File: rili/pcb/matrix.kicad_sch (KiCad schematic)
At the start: 144 parts, among them J5 MJ-4PP-9, P5 i2c-pin, P6 i2c-pin, SW100 SW_PUSH, SW101 SW_PUSH, SW102 SW_PUSH, SW103 SW_PUSH, SW104 SW_PUSH, SW105 SW_PUSH, SW54 SW_PUSH, SW55 SW_PUSH, SW56 SW_PUSH, SW57 SW_PUSH, SW58 SW_PUSH, SW59 SW_PUSH, SW60 SW_PUSH, SW61 SW_PUSH, SW62 SW_PUSH, SW63 SW_PUSH, SW64 SW_PUSH, SW65 SW_PUSH, SW66 SW_PUSH, SW67 SW_PUSH, SW68 SW_PUSH, SW69 SW_PUSH, SW70 SW_PUSH, SW71 SW_PUSH, SW72 SW_PUSH, SW73 SW_PUSH, SW74 SW_PUSH, SW75 SW_PUSH, SW76 SW_PUSH, SW77 SW_PUSH, SW78 SW_PUSH, SW79 SW_PUSH, SW80 SW_PUSH, SW81 SW_PUSH, SW82 SW_PUSH, SW83 SW_PUSH, SW84 SW_PUSH, SW85 SW_PUSH, SW86 SW_PUSH, SW87 SW_PUSH, SW88 SW_PUSH, SW89 SW_PUSH, SW90 SW_PUSH, SW91 SW_PUSH, SW92 SW_PUSH, SW93 SW_PUSH, SW94 SW_PUSH, SW95 SW_PUSH, SW96 SW_PUSH, SW97 SW_PUSH, SW98 SW_PUSH, SW99 SW_PUSH, U11 D, U12 D, U13 D, U14 D

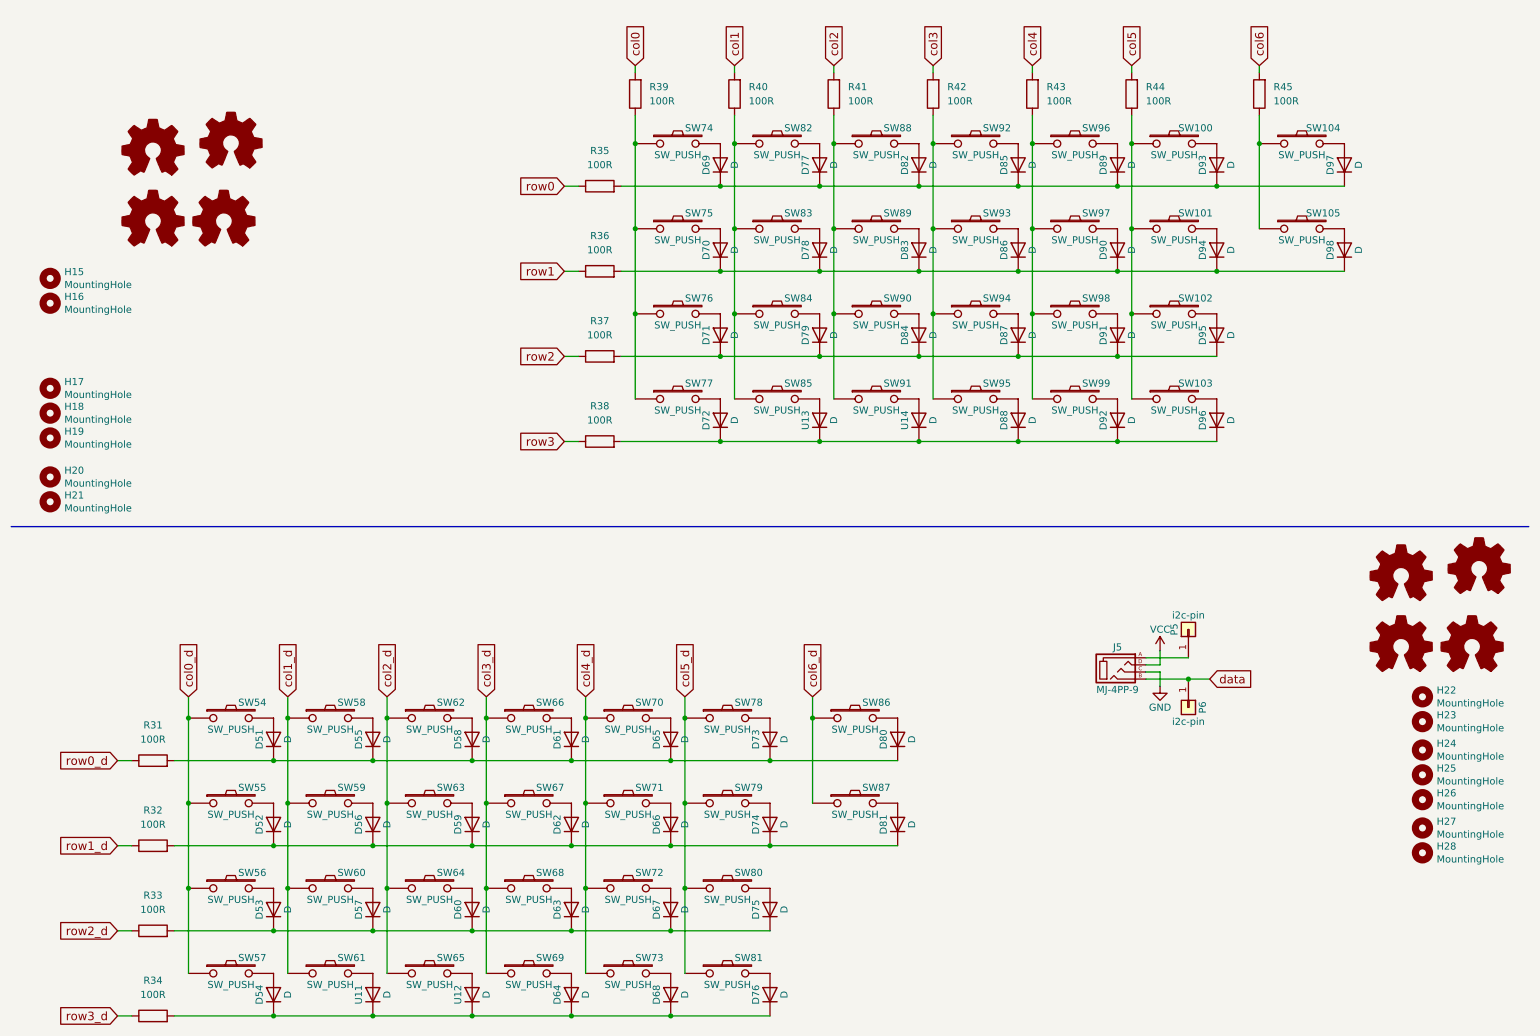
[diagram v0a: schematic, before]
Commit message: schéma v2 : coffre P4 complet — ERC 0 erreur
- Feuille p4 (ex sans_titre) : AMS1117-3.3 (rail P4_3V3 séparé, 10µF/22µF),
  CHIP_PU RC 100k+100nF, USB HS (ESP_USB_P/N) vers le port 2 du hub,
  microSD slot UHS-I (CLK/CMD/DAT0-3 sur GPIO39-44, pull-ups 10k),
  prog P4 via port 3 du hub (USB-Serial-JTAG + jumpers d'isolation)
- Périphériques : écran Sharp LS011B7DH03 (SPI partagé, CS_DPL=GPIO14),
  trackpad TPS43 (I2C 47/48, RDY=42, bloc généré+validé), C6 laissé vierge
  (OTA via P4 = voie officielle)
- Ménage ERC : 65 no_connect + 6 PWR_FLAG posés par script (fix_nc.py),
  labels fantômes S3P4 supprimés — ERC projet : 71 → 0 erreur,
  warnings 262 → 158 (ratchet enregistré)
- Hooks Claude Code Stop/PostToolUse désactivés (garde-fou = pre-push + CI)

Reste au schéma : le 2e MCU (moitié droite, col*_d/row*_d en attente).
DRC layout hors périmètre (chantier séparé).

Co-Authored-By: Claude Fable 5 <noreply@anthropic.com>
Claude-Session: https://claude.ai/code/session_01GfX5RmekmQi78Dm37qsT4Z
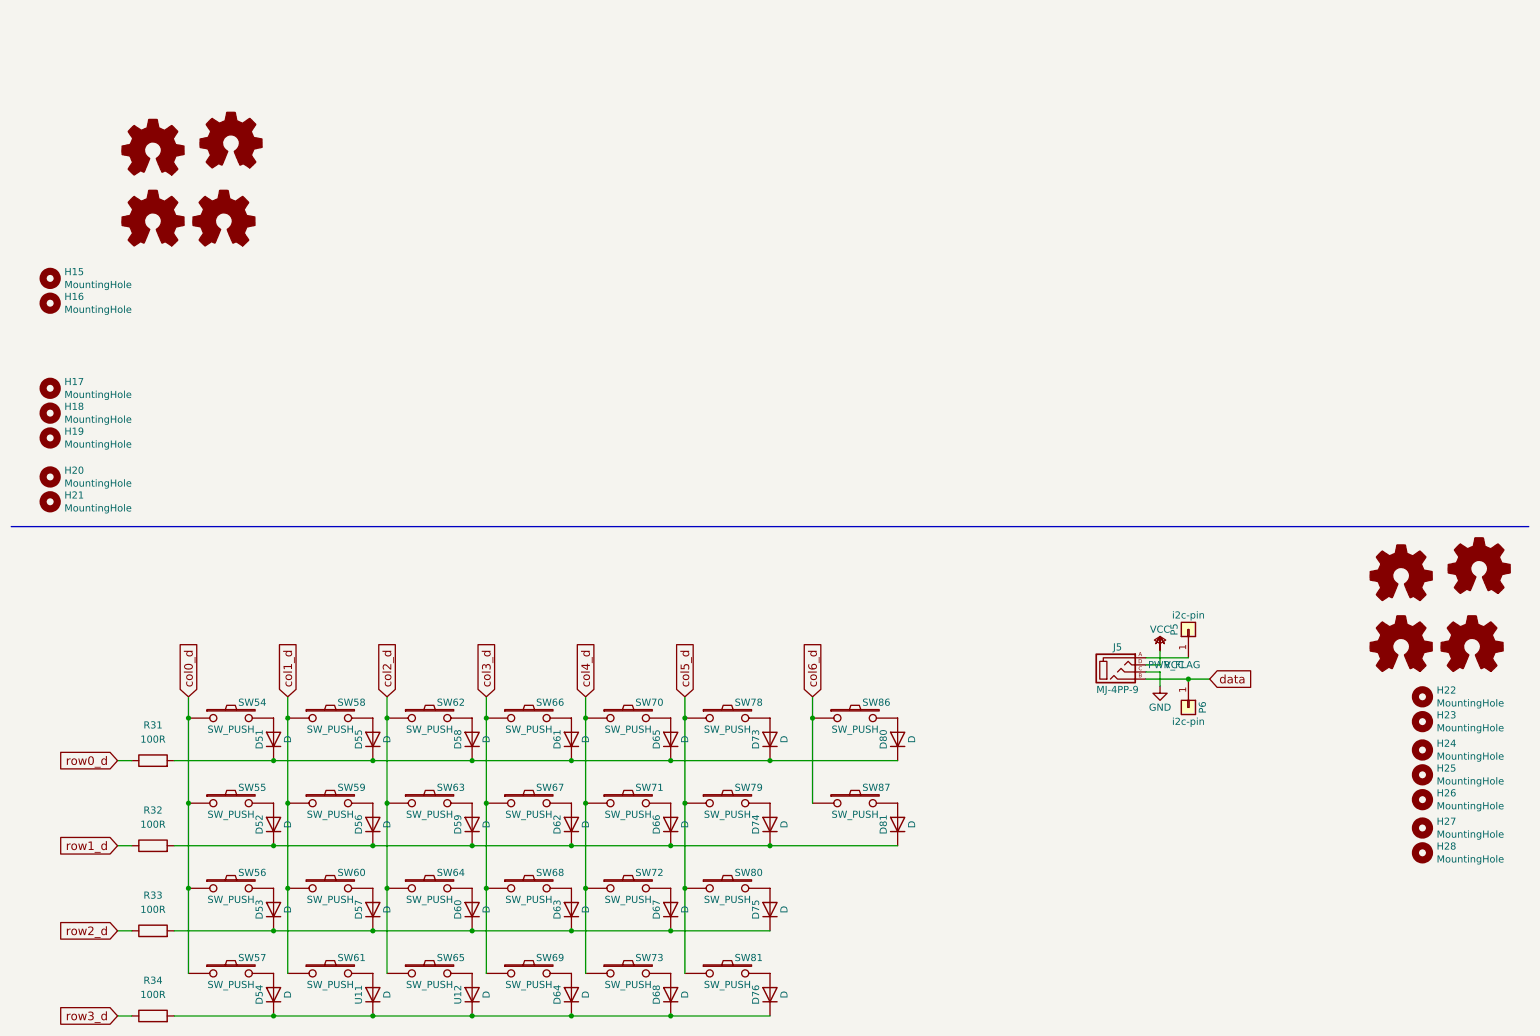
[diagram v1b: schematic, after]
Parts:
- removed D69, D70, D71, D72, D77, D78, D79, D82, D83, D84, D85, D86, D87, D88, D89, D90, D91, D92, D93, D94, D95, D96, D97, D98, U13, U14: D, EKR82-footprint:Diode_TH_SOD123EKR, symbol Device:D
- removed R35, R36, R37, R38, R39, R40, R41, R42, R43, R44, R45: 100R, Resistor_SMD:R_0603_1608Metric_Pad0.98x0.95mm_HandSolder, symbol Device:R
- removed SW100, SW101, SW102, SW103, SW104, SW105, SW74, SW75, SW76, SW77, SW82, SW83, SW84, SW85, SW88, SW89, SW90, SW91, SW92, SW93, SW94, SW95, SW96, SW97, SW98, SW99: SW_PUSH, PMW3360:SW_Hotswap_Kailh_Choc_V1V2_1.00u, symbol corne-cherry-rescue:SW_PUSH-kbd-corne-cherry-rescue
